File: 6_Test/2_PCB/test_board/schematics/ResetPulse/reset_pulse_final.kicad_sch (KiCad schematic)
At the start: 3 parts

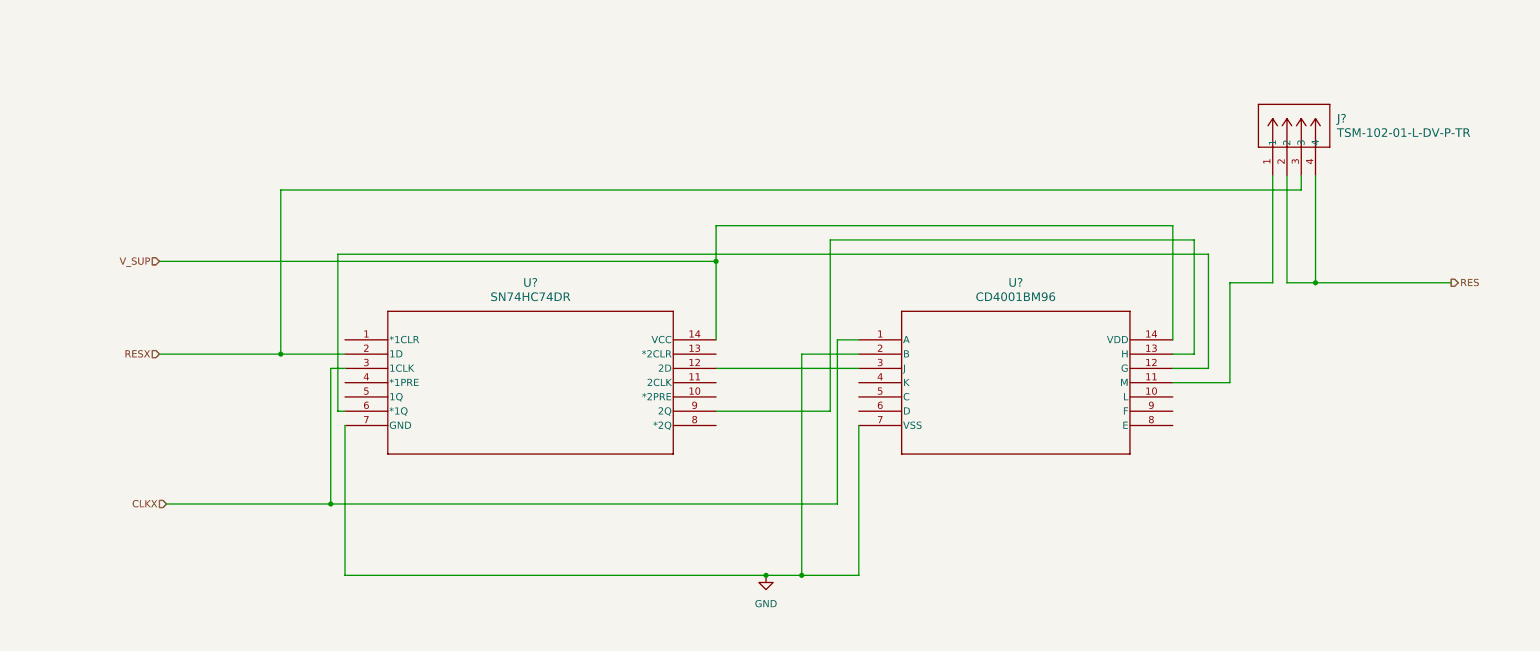
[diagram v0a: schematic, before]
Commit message: made changes with accordance to feedback. Remvoed excess files.
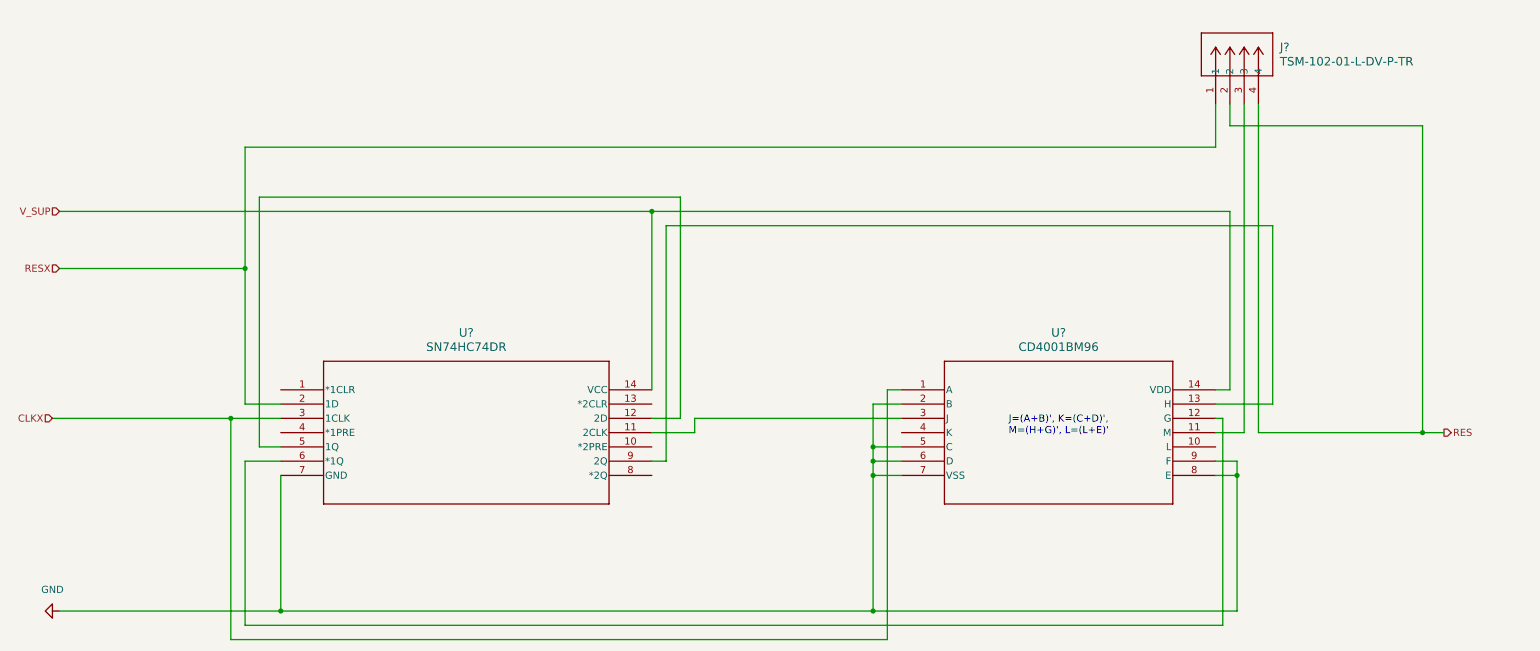
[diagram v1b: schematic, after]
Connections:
- net GND: now also U?.5 (C), U?.6 (D), U?.8 (E), U?.9 (F)
- net RESX: now also J?.1; no longer J?.3
- net at U?.11 (M): now also J?.3; no longer J?.1
- net at U?.3 (J): now also U?.11 (2CLK); no longer U?.12 (2D)
- net at U?.5 (1Q): now also U?.12 (2D)
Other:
- note added: "J=(A+B)', K=(C+D)', M=(H+G)', L=(L+E)'"
- moved on the sheet: J?, U?

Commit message: Edits 112524
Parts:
- added C31, C33: 4.7u, Cap4.7uFFootprints:CAP_0603_CL10A_1P6XP8_SAM, symbol Device:C
- added C32, C34: 100n, cap100nFFootprints:CAP_CL05_SAM, symbol Device:C
- added J12: Reset_PWR_Jumpers, Connector_PinHeader_2.54mm:PinHeader_2x02_P2.54mm_Vertical, symbol 2x2Header:TSM-102-01-L-DV-P-TR
- J13: renamed from J?; value TSM-102-01-L-DV-P-TR -> Reset_Signal_Jumpers; footprint CONN_TSM-102-01-L-DV-P-TR_SAI -> Connector_PinHeader_2.54mm:PinHeader_2x02_P2.54mm_Vertical
- U?: footprint D14 -> ECE628_lib:nor_gate_D14
- U?: footprint D14 -> ECE628_lib:flip_flop_D14
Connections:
- net GND: now also C31.2, C32.2, C33.1, C34.1
- net V_SUP: now also J12.1, J12.3; no longer U?.14 (VCC), U?.14 (VDD)
- net at U?.1 (*1CLR): now also U?.10 (*2PRE), U?.13 (*2CLR), U?.14 (VCC), U?.4 (*1PRE), C31.1, C32.1, J12.2
- new net: C33.2, C34.2, J12.4, U?.14 (VDD)

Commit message: final draft of board, revision 2
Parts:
- C31, C33: footprint Cap4.7uFFootprints:CAP_0603_CL10A_1P6XP8_SAM -> Capacitor_SMD:C_0603_1608Metric
- C32, C34: footprint cap100nFFootprints:CAP_CL05_SAM -> Capacitor_SMD:C_0402_1005Metric
- J12, J13: footprint Connector_PinHeader_2.54mm:PinHeader_2x02_P2.54mm_Vertical -> ECE628_lib:2x2Header
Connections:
- net V_SUP renamed IOVDD
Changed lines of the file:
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@@
 		)
 	)
-	(hierarchical_label "V_SUP"
+	(hierarchical_label "IOVDD"
 		(shape input)
 		(at 27.94 41.91 180)
@@
 			)
 		)
-		(property "Footprint" "Connector_PinHeader_2.54mm:PinHeader_2x02_P2.54mm_Vertical"
+		(property "Footprint" "ECE628_lib:2x2Header"
 			(at 60.96 39.37 0)
 			(effects
@@
 			)
 		)
-		(property "Footprint" "cap100nFFootprints:CAP_CL05_SAM"
+		(property "Footprint" "Capacitor_SMD:C_0402_1005Metric"
 			(at 71.12 56.8452 0)
 			(effects
@@
 			)
 		)
-		(property "Footprint" "Cap4.7uFFootprints:CAP_0603_CL10A_1P6XP8_SAM"
+		(property "Footprint" "Capacitor_SMD:C_0603_1608Metric"
 			(at 53.34 46.6852 0)
 			(effects
@@
 			)
 		)
-		(property "Footprint" "cap100nFFootprints:CAP_CL05_SAM"
+		(property "Footprint" "Capacitor_SMD:C_0402_1005Metric"
 			(at 53.34 56.8452 0)
 			(effects
@@
 			)
 		)
-		(property "Footprint" "Cap4.7uFFootprints:CAP_0603_CL10A_1P6XP8_SAM"
+		(property "Footprint" "Capacitor_SMD:C_0603_1608Metric"
 			(at 71.12 46.6852 0)
 			(effects
@@
 			)
 		)
-		(property "Footprint" "Connector_PinHeader_2.54mm:PinHeader_2x02_P2.54mm_Vertical"
+		(property "Footprint" "ECE628_lib:2x2Header"
 			(at 232.41 43.18 0)
 			(effects

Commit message: Edit Layout 1_27
Rearranged the components in the layout and added majority of traces and ground layer. AVSS connections still need to be connected along with IOVDD
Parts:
- J12, J13: footprint ECE628_lib:2x2Header -> Connector_PinHeader_2.54mm:PinHeader_2x02_P2.54mm_Vertical
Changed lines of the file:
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@@
 			)
 		)
-		(property "Footprint" "ECE628_lib:2x2Header"
+		(property "Footprint" "Connector_PinHeader_2.54mm:PinHeader_2x02_P2.54mm_Vertical"
 			(at 60.96 39.37 0)
 			(effects
@@
 			)
 		)
-		(property "Footprint" "ECE628_lib:2x2Header"
+		(property "Footprint" "Connector_PinHeader_2.54mm:PinHeader_2x02_P2.54mm_Vertical"
 			(at 232.41 43.18 0)
 			(effects

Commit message: Finished board layout
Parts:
- renumbered C31 to C27, C32 to C28, C33 to C29, C34 to C30
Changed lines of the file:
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@@
 		(on_board yes)
 		(dnp no)
-		(property "Reference" "C34"
+		(property "Reference" "C30"
 			(at 72.898 59.69 90)
 			(effects
@@
 			(project "board_main"
 				(path "/9c0580c5-7bd5-4e54-bf4c-826aa4ac3630/9621bf7e-7afb-4298-8f88-3144a5d5b439"
-					(reference "C34")
+					(reference "C30")
 					(unit 1)
 				)
@@
 		(on_board yes)
 		(dnp no)
-		(property "Reference" "C31"
+		(property "Reference" "C27"
 			(at 54.864 49.276 90)
 			(effects
@@
 			(project "board_main"
 				(path "/9c0580c5-7bd5-4e54-bf4c-826aa4ac3630/9621bf7e-7afb-4298-8f88-3144a5d5b439"
-					(reference "C31")
+					(reference "C27")
 					(unit 1)
 				)
@@
 		(on_board yes)
 		(dnp no)
-		(property "Reference" "C32"
+		(property "Reference" "C28"
 			(at 55.118 59.69 90)
 			(effects
@@
 			(project "board_main"
 				(path "/9c0580c5-7bd5-4e54-bf4c-826aa4ac3630/9621bf7e-7afb-4298-8f88-3144a5d5b439"
-					(reference "C32")
+					(reference "C28")
 					(unit 1)
 				)
@@
 		(on_board yes)
 		(dnp no)
-		(property "Reference" "C33"
+		(property "Reference" "C29"
 			(at 72.644 49.276 90)
 			(effects
@@
 			(project "board_main"
 				(path "/9c0580c5-7bd5-4e54-bf4c-826aa4ac3630/9621bf7e-7afb-4298-8f88-3144a5d5b439"
-					(reference "C33")
-					(unit 1)
-				)
+					(reference "C29")
+					(unit 1)
+				)
